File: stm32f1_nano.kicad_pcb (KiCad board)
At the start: 2 copper layers, 43.2 x 17.8 mm, 45 parts, among them J1 Analog, J2 Digital, J3 TYPE-C-31-M-12, J5 DEBUG, U1 STM32F103C8T6, U2 W25Q128JVSIQ, U4 XC6206P332MR, U5 AMS1117-5.0, Y1 X322516MLB4SI

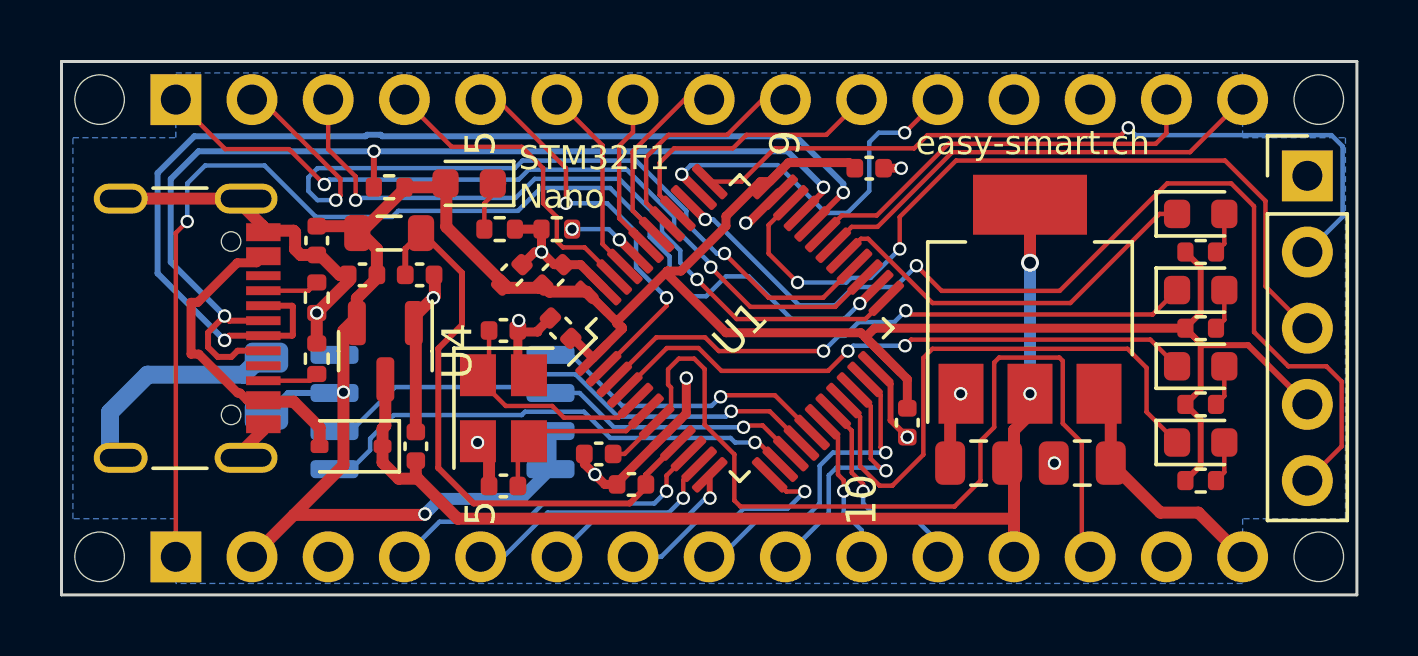
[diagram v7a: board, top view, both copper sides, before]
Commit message: #7 Change W25 for a SST26
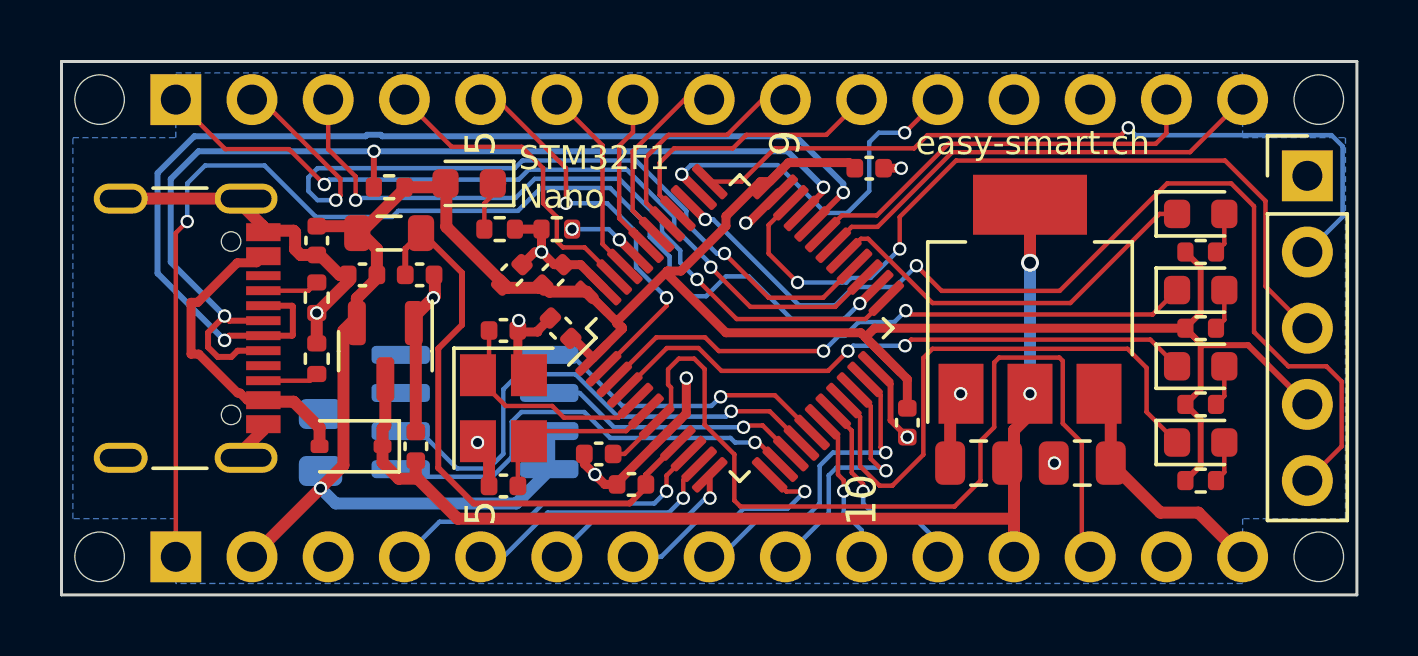
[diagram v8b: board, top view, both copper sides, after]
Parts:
- C12: value 100n 100V -> 100nF
- U2: value W25Q128JVSIQ -> SST26VF016BEUI-104I/SN; footprint Package_SO:SOIC-8_5.23x5.23mm_P1.27mm -> Package_SO:SOIC-8_3.9x4.9mm_P1.27mm
- moved C12 2.60 mm to (108.6, 94.9)
- moved U2 1.08 mm to (113.8, 93.9)
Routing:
- net GND: track 48.3 -> 40.9 mm
- net +3.3V: track 88.8 -> 85.9 mm, vias 2 -> 1
- net /SPI1_NSS: track 16.0 -> 15.1 mm
- net /SPI1_MISO: track 16.9 -> 17.5 mm
